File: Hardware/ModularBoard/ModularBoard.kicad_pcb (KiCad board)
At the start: 2 copper layers, 27.9 x 15.2 mm, 2 parts, among them IC1 ATTINY85-P, J1 GSG-USB-MICRO-B

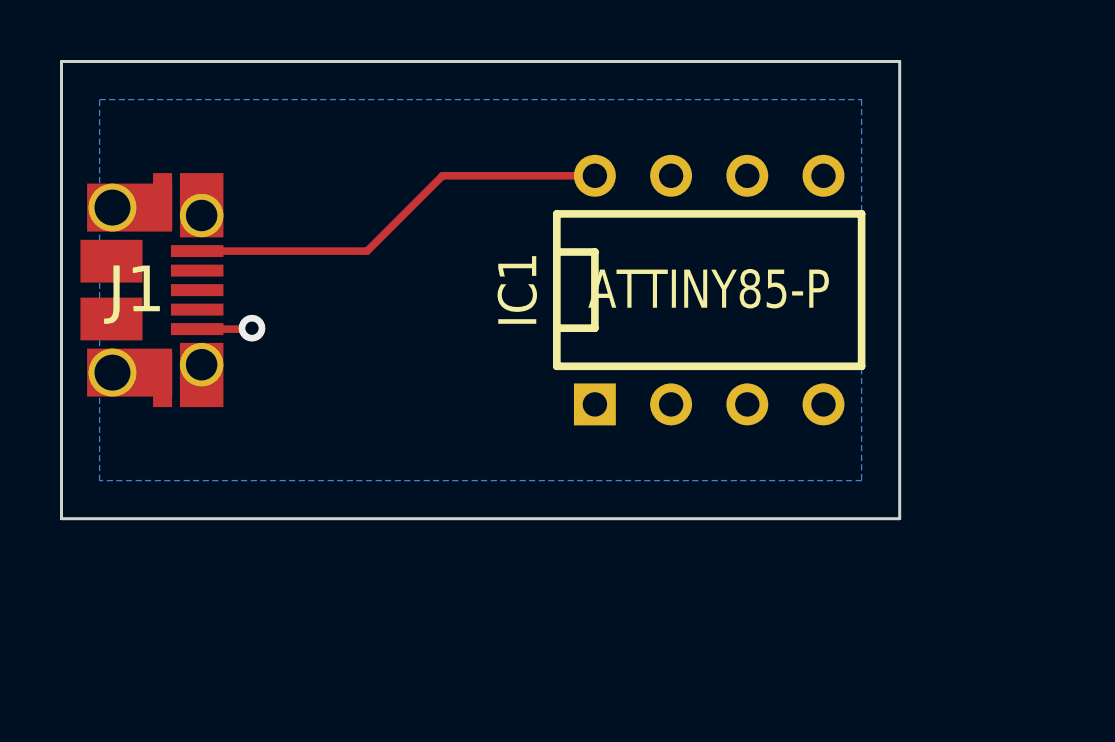
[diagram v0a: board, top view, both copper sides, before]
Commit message: Updated schematic, should just need a few more breakout pins, maybe caps for filtering
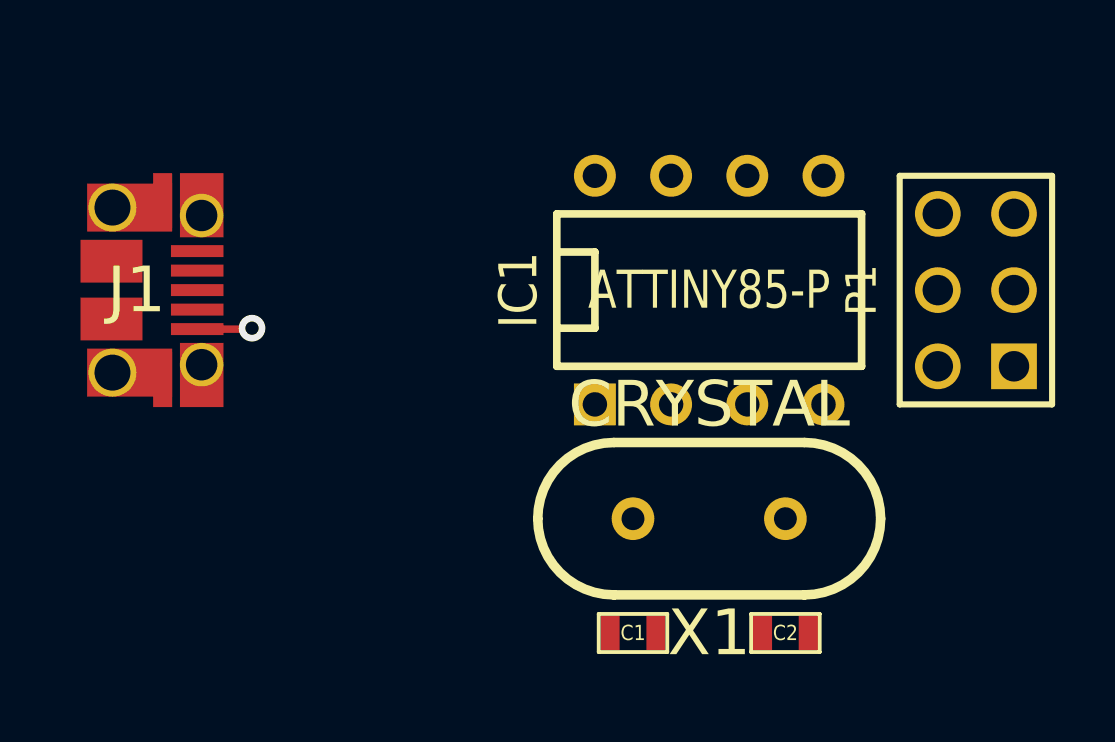
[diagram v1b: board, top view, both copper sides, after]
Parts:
- added C1: CP1, SM0603, F.Cu at (223.5, 161.3)
- added C2: CP1, SM0603, F.Cu at (228.6, 161.3)
- added P1: CONN_3X2, pin_array_3x2, F.Cu at (234.9, 149.9)
- added X1: CRYSTAL, HC-49V, F.Cu at (226.1, 157.5)
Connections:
- IC1 pad 1: (no net) -> /RESET
- IC1 pad 2: (no net) -> N-000006
- IC1 pad 3: (no net) -> N-0000012
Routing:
- net +5V: track 14.3 -> 0.00 mm
- removed copper zone on B.Cu, net GND
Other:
- board outline removed
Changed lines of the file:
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@@
 (kicad_pcb (version 3) (host pcbnew "(2013-07-07 BZR 4022)-stable")
   (general
-    (links 2)
-    (no_connects 0)
-    (area 193.86296 142.189999 232.460001 157.530001)
+    (links 11)
+    (no_connects 11)
+    (area 204.419999 142.189999 232.460001 157.530001)
     (thickness 1.6)
-    (drawings 4)
-    (tracks 6)
+    (drawings 0)
+    (tracks 3)
     (zones 0)
-    (modules 2)
-    (nets 3)
+    (modules 6)
+    (nets 6)
   )
   (page A3)
@@
   (net 0 "")
   (net 1 +5V)
-  (net 2 GND)
+  (net 2 /RESET)
+  (net 3 GND)
+  (net 4 N-0000012)
+  (net 5 N-000006)
   (net_class Default "This is the default net class."
     (clearance 0.254)
@@
     (add_net "")
     (add_net +5V)
+    (add_net /RESET)
     (add_net GND)
+    (add_net N-0000012)
+    (add_net N-000006)
   )
   (net_class Power ""
@@
     (pad 1 thru_hole rect (at -3.81 3.81) (size 1.397 1.397) (drill 0.8128)
       (layers *.Cu *.Mask F.SilkS)
+      (net 2 /RESET)
     )
     (pad 2 thru_hole circle (at -1.27 3.81) (size 1.397 1.397) (drill 0.8128)
       (layers *.Cu *.Mask F.SilkS)
+      (net 5 N-000006)
     )
     (pad 3 thru_hole circle (at 1.27 3.81) (size 1.397 1.397) (drill 0.8128)
       (layers *.Cu *.Mask F.SilkS)
+      (net 4 N-0000012)
     )
     (pad 4 thru_hole circle (at 3.81 3.81) (size 1.397 1.397) (drill 0.8128)
       (layers *.Cu *.Mask F.SilkS)
-      (net 2 GND)
+      (net 3 GND)
     )
     (pad 5 thru_hole circle (at 3.81 -3.81) (size 1.397 1.397) (drill 0.8128)
@@
     (pad 5 smd rect (at 4.52374 1.30048) (size 1.75006 0.39878)
       (layers F.Cu F.Paste F.Mask)
-      (net 2 GND)
+      (net 3 GND)
       (die_length 0.04064)
       (solder_mask_margin 0.1016)
@@
     )
   )
-  (gr_line (start 232.41 142.24) (end 204.47 142.24) (angle 90) (layer Edge.Cuts) (width 0.1))
-  (gr_line (start 232.41 157.48) (end 232.41 142.24) (angle 90) (layer Edge.Cuts) (width 0.1))
-  (gr_line (start 204.47 157.48) (end 232.41 157.48) (angle 90) (layer Edge.Cuts) (width 0.1))
-  (gr_line (start 204.47 142.24) (end 204.47 157.48) (angle 90) (layer Edge.Cuts) (width 0.1))
-  (segment (start 208.99374 148.55952) (end 214.66048 148.55952) (width 0.254) (layer F.Cu) (net 1) (status 400000))
-  (segment (start 217.17 146.05) (end 222.25 146.05) (width 0.254) (layer F.Cu) (net 1) (status 800000))
-  (segment (start 214.66048 148.55952) (end 217.17 146.05) (width 0.254) (layer F.Cu) (net 1))
-  (segment (start 208.99374 151.16048) (end 210.78952 151.16048) (width 0.254) (layer F.Cu) (net 2) (status 400000))
-  (via (at 210.82 151.13) (size 0.889) (layers F.Cu B.Cu) (net 2))
-  (segment (start 210.78952 151.16048) (end 210.82 151.13) (width 0.254) (layer F.Cu) (net 2))
-  (zone (net 2) (net_name GND) (layer B.Cu) (hatch edge 0.508)
-    (connect_pads (clearance 0.508))
-    (min_thickness 0.254)
-    (fill (arc_segments 16) (thermal_gap 0.508) (thermal_bridge_width 0.508))
-    (polygon
-      (pts
-        (xy 205.74 143.51) (xy 231.14 143.51) (xy 231.14 156.21) (xy 205.74 156.21)
-      )
-    )
-  )
+  (module SM0603 (layer F.Cu)
+    (at 223.52 161.29)
+    (attr smd)
+    (fp_text reference C1 (at 0 0) (layer F.SilkS)
+      (effects (font (size 0.508 0.4572) (thickness 0.1143)))
+    )
+    (fp_text value CP1 (at 0 0) (layer F.SilkS) hide
+      (effects (font (size 0.508 0.4572) (thickness 0.1143)))
+    )
+    (fp_line (start -1.143 -0.635) (end 1.143 -0.635) (layer F.SilkS) (width 0.127))
+    (fp_line (start 1.143 -0.635) (end 1.143 0.635) (layer F.SilkS) (width 0.127))
+    (fp_line (start 1.143 0.635) (end -1.143 0.635) (layer F.SilkS) (width 0.127))
+    (fp_line (start -1.143 0.635) (end -1.143 -0.635) (layer F.SilkS) (width 0.127))
+    (pad 1 smd rect (at -0.762 0) (size 0.635 1.143)
+      (layers F.Cu F.Paste F.Mask)
+      (net 5 N-000006)
+    )
+    (pad 2 smd rect (at 0.762 0) (size 0.635 1.143)
+      (layers F.Cu F.Paste F.Mask)
+      (net 3 GND)
+    )
+    (model smd\resistors\R0603.wrl
+      (at (xyz 0 0 0.001))
+      (scale (xyz 0.5 0.5 0.5))
+      (rotate (xyz 0 0 0))
+    )
+  )
+  (module SM0603 (layer F.Cu)
+    (at 228.6 161.29 180)
+    (attr smd)
+    (fp_text reference C2 (at 0 0 180) (layer F.SilkS)
+      (effects (font (size 0.508 0.4572) (thickness 0.1143)))
+    )
+    (fp_text value CP1 (at 0 0 180) (layer F.SilkS) hide
+      (effects (font (size 0.508 0.4572) (thickness 0.1143)))
+    )
+    (fp_line (start -1.143 -0.635) (end 1.143 -0.635) (layer F.SilkS) (width 0.127))
+    (fp_line (start 1.143 -0.635) (end 1.143 0.635) (layer F.SilkS) (width 0.127))
+    (fp_line (start 1.143 0.635) (end -1.143 0.635) (layer F.SilkS) (width 0.127))
+    (fp_line (start -1.143 0.635) (end -1.143 -0.635) (layer F.SilkS) (width 0.127))
+    (pad 1 smd rect (at -0.762 0 180) (size 0.635 1.143)
+      (layers F.Cu F.Paste F.Mask)
+      (net 4 N-0000012)
+    )
+    (pad 2 smd rect (at 0.762 0 180) (size 0.635 1.143)
+      (layers F.Cu F.Paste F.Mask)
+      (net 3 GND)
+    )
+    (model smd\resistors\R0603.wrl
+      (at (xyz 0 0 0.001))
+      (scale (xyz 0.5 0.5 0.5))
+      (rotate (xyz 0 0 0))
+    )
+  )
+  (module pin_array_3x2 (layer F.Cu)
+    (at 234.95 149.86 90)
+    (descr "Double rangee de contacts 2 x 4 pins")
+    (tags CONN)
+    (fp_text reference P1 (at 0 -3.81 90) (layer F.SilkS)
+      (effects (font (size 1.016 1.016) (thickness 0.2032)))
+    )
+    (fp_text value CONN_3X2 (at 0 3.81 90) (layer F.SilkS) hide
+      (effects (font (size 1.016 1.016) (thickness 0.2032)))
+    )
+    (fp_line (start 3.81 2.54) (end -3.81 2.54) (layer F.SilkS) (width 0.2032))
+    (fp_line (start -3.81 -2.54) (end 3.81 -2.54) (layer F.SilkS) (width 0.2032))
+    (fp_line (start 3.81 -2.54) (end 3.81 2.54) (layer F.SilkS) (width 0.2032))
+    (fp_line (start -3.81 2.54) (end -3.81 -2.54) (layer F.SilkS) (width 0.2032))
+    (pad 1 thru_hole rect (at -2.54 1.27 90) (size 1.524 1.524) (drill 1.016)
+      (layers *.Cu *.Mask F.SilkS)
+      (net 2 /RESET)
+    )
+    (pad 2 thru_hole circle (at -2.54 -1.27 90) (size 1.524 1.524) (drill 1.016)
+      (layers *.Cu *.Mask F.SilkS)
+      (net 3 GND)
+    )
+    (pad 3 thru_hole circle (at 0 1.27 90) (size 1.524 1.524) (drill 1.016)
+      (layers *.Cu *.Mask F.SilkS)
+    )
+    (pad 4 thru_hole circle (at 0 -1.27 90) (size 1.524 1.524) (drill 1.016)
+      (layers *.Cu *.Mask F.SilkS)
+    )
+    (pad 5 thru_hole circle (at 2.54 1.27 90) (size 1.524 1.524) (drill 1.016)
+      (layers *.Cu *.Mask F.SilkS)
+    )
+    (pad 6 thru_hole circle (at 2.54 -1.27 90) (size 1.524 1.524) (drill 1.016)
+      (layers *.Cu *.Mask F.SilkS)
+      (net 1 +5V)
+    )
+    (model pin_array/pins_array_3x2.wrl
+      (at (xyz 0 0 0))
+      (scale (xyz 1 1 1))
+      (rotate (xyz 0 0 0))
+    )
+  )
+  (module HC-49V (layer F.Cu)
+    (at 226.06 157.48 180)
+    (descr "Quartz boitier HC-49 Vertical")
+    (tags "QUARTZ DEV")
+    (autoplace_cost180 10)
+    (fp_text reference X1 (at 0 -3.81 180) (layer F.SilkS)
+      (effects (font (size 1.524 1.524) (thickness 0.3048)))
+    )
+    (fp_text value CRYSTAL (at 0 3.81 180) (layer F.SilkS)
+      (effects (font (size 1.524 1.524) (thickness 0.3048)))
+    )
+    (fp_line (start -3.175 2.54) (end 3.175 2.54) (layer F.SilkS) (width 0.3175))
+    (fp_line (start -3.175 -2.54) (end 3.175 -2.54) (layer F.SilkS) (width 0.3175))
+    (fp_arc (start 3.175 0) (end 3.175 -2.54) (angle 90) (layer F.SilkS) (width 0.3175))
+    (fp_arc (start 3.175 0) (end 5.715 0) (angle 90) (layer F.SilkS) (width 0.3175))
+    (fp_arc (start -3.175 0) (end -5.715 0) (angle 90) (layer F.SilkS) (width 0.3175))
+    (fp_arc (start -3.175 0) (end -3.175 2.54) (angle 90) (layer F.SilkS) (width 0.3175))
+    (pad 1 thru_hole circle (at -2.54 0 180) (size 1.4224 1.4224) (drill 0.762)
+      (layers *.Cu *.Mask F.SilkS)
+      (net 4 N-0000012)
+    )
+    (pad 2 thru_hole circle (at 2.54 0 180) (size 1.4224 1.4224) (drill 0.762)
+      (layers *.Cu *.Mask F.SilkS)
+      (net 5 N-000006)
+    )
+    (model discret/xtal/crystal_hc18u_vertical.wrl
+      (at (xyz 0 0 0))
+      (scale (xyz 1 1 0.2))
+      (rotate (xyz 0 0 0))
+    )
+  )
+  (segment (start 208.99374 151.16048) (end 210.78952 151.16048) (width 0.254) (layer F.Cu) (net 3))
+  (via (at 210.82 151.13) (size 0.889) (layers F.Cu B.Cu) (net 3))
+  (segment (start 210.78952 151.16048) (end 210.82 151.13) (width 0.254) (layer F.Cu) (net 3))
 )

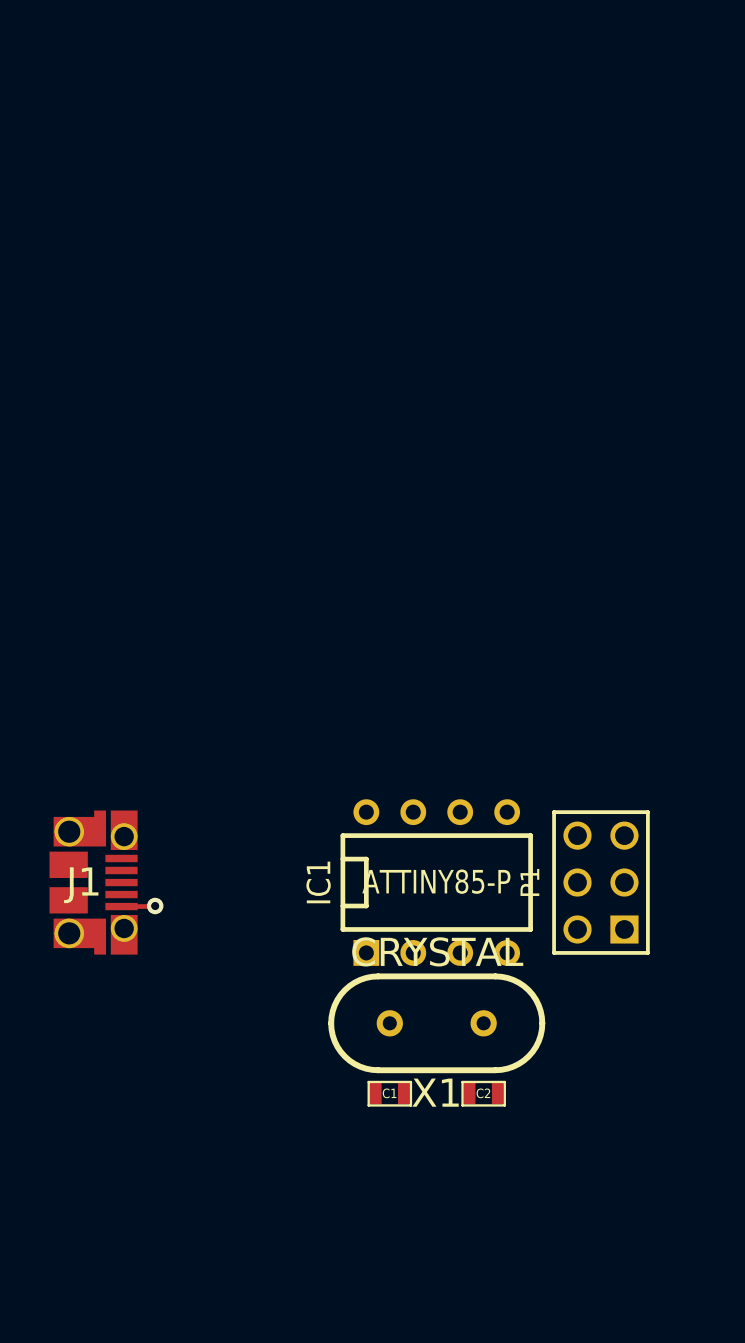
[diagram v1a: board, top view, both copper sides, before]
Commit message: Schematic should be done, board partially implemented
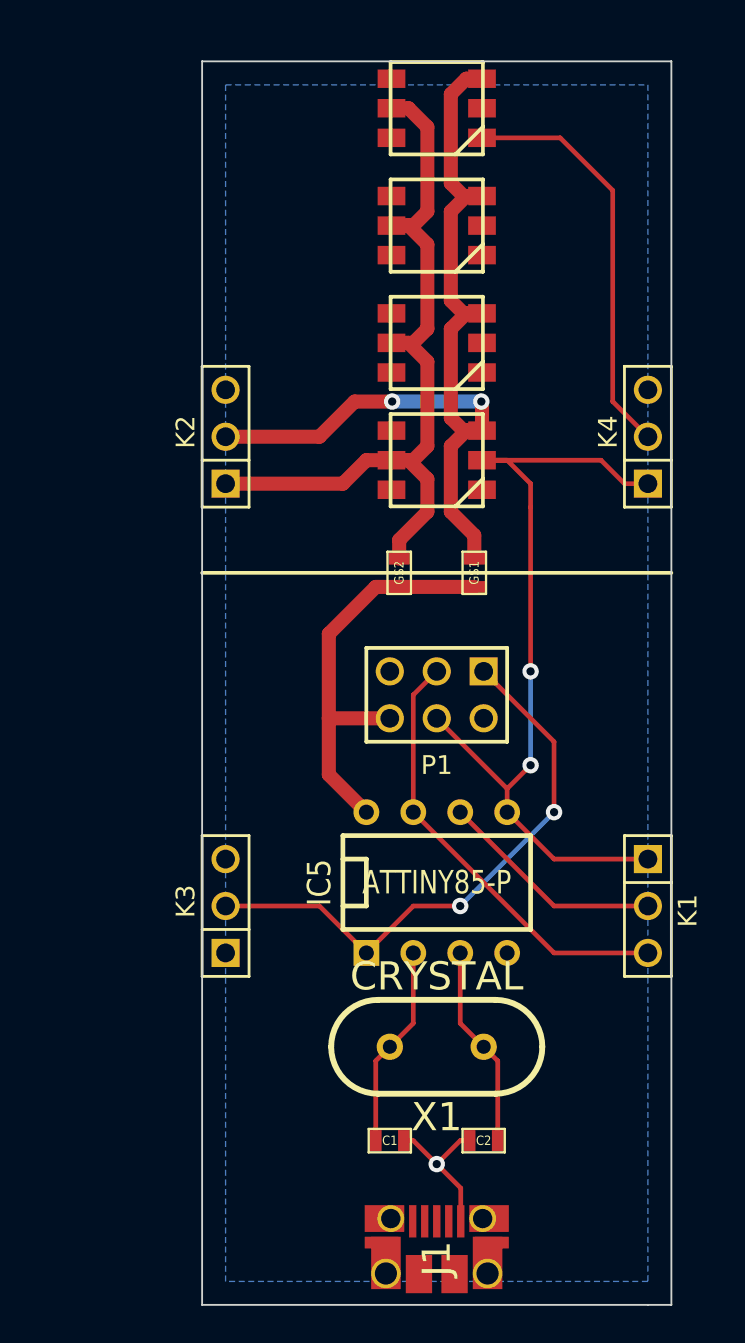
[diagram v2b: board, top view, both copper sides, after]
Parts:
- added GS1: GS2, SM0603, F.Cu at (228.1, 133.1)
- added GS2: GS2, SM0603, F.Cu at (224.0, 133.1)
- added IC2: WS2811-5050, WS2811-5050, F.Cu at (226.1, 120.7)
- added IC3: WS2811-5050, WS2811-5050, F.Cu at (226.1, 114.3)
- added IC4: WS2811-5050, WS2811-5050, F.Cu at (226.1, 108.0)
- added IC5: ATTINY85-P, DIP-8__300, F.Cu at (226.1, 149.9)
- added K1: CONN_3, PIN_ARRAY_3X1, F.Cu at (237.5, 151.1)
- added K2: CONN_3, PIN_ARRAY_3X1, F.Cu at (214.6, 125.7)
- added K3: CONN_3, PIN_ARRAY_3X1, F.Cu at (214.6, 151.1)
- added K4: CONN_3, PIN_ARRAY_3X1, F.Cu at (237.5, 125.7)
- IC1: value ATTINY85-P -> WS2811-5050; footprint DIP-8__300 -> WS2811-5050
- moved J1 31.4 mm to (226.1, 172.7), turned to 90 degrees
- moved IC1 22.9 mm to (226.1, 127.0)
- moved P1 13.5 mm to (226.1, 139.7), turned to 180 degrees
- moved C1 2.54 mm to (223.5, 163.8)
- moved C2 2.54 mm to (228.6, 163.8)
- moved X1 1.27 mm to (226.1, 158.8)
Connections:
- C1 pad 1: N-000006 -> N-0000017
- C2 pad 1: N-0000012 -> N-0000018
- IC1 pad 1: /RESET -> N-000003
- IC1 pad 2: N-000006 -> /MOSI
- IC1 pad 3: N-0000012 -> VCC
- IC1 pad 4: GND -> (no net)
- IC1 pad 5: (no net) -> VDD
- IC1 pad 6: (no net) -> GND
- P1 pad 3: (no net) -> /SCK
- P1 pad 4: (no net) -> /MOSI
- P1 pad 5: (no net) -> /MISO
- X1 pad 1: N-0000012 -> N-0000018
- X1 pad 2: N-000006 -> N-0000017
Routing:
- net VCC: track 0.00 -> 51.4 mm, vias 0 -> 2
- net /MOSI: track 0.00 -> 45.0 mm, vias 0 -> 2
- net VDD: track 0.00 -> 44.4 mm
- net /RESET: track 0.00 -> 31.2 mm, vias 0 -> 2
- net /SCK: track 0.00 -> 24.0 mm
- net +5V: track 0.00 -> 22.7 mm
- net /DO: track 0.00 -> 22.4 mm
- net /MISO: track 0.00 -> 12.3 mm
- net N-0000018: track 0.00 -> 11.0 mm
- net N-0000017: track 0.00 -> 11.0 mm
- net GND: track 1.84 -> 8.24 mm
- added copper zone on B.Cu, net GND
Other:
- board outline added: 25.4 x 67.3 mm

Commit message: board should be done, save trace width tweaking
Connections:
- K3 pad 1: VCC -> +5V
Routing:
- net +5V: track 22.7 -> 57.5 mm, vias 0 -> 2
- net /MISO: track 12.3 -> 26.6 mm, vias 0 -> 2
- net N-000002: track 0.00 -> 13.1 mm, vias 0 -> 2
- net N-0000012: track 0.00 -> 12.6 mm, vias 0 -> 2
- net N-0000013: track 0.00 -> 11.0 mm, vias 0 -> 2
- net GND: track 8.24 -> 16.0 mm, vias 1 -> 5
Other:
- board size 25.4 x 67.3 mm -> 25.4 x 68.6 mm
- net class USB 5V added: clearance 0.254, trace_width 0.381, via_dia 0.889, via_drill 0.635
